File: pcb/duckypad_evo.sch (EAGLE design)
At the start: 93 parts, among them IC1 STM32F072C8T6, IC2 REG1117, IC3 74AHCT1G08DBV, SW1 324_SW324_SWITCH_FOOT_HOLE, SW10 KAILH_SWITCH_SOCKET_KAILH_SWI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, SW11 KAILH_SWITCH_SOCKET_KAILH_SWI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, SW12 KAILH_SWITCH_SOCKET_KAILH_SWI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, SW13 KAILH_SWITCH_SOCKET_KAILH_SWI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, SW14 KAILH_SWITCH_SOCKET_KAILH_SWI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, SW15 KAILH_SWITCH_SOCKET_KAILH_SWI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

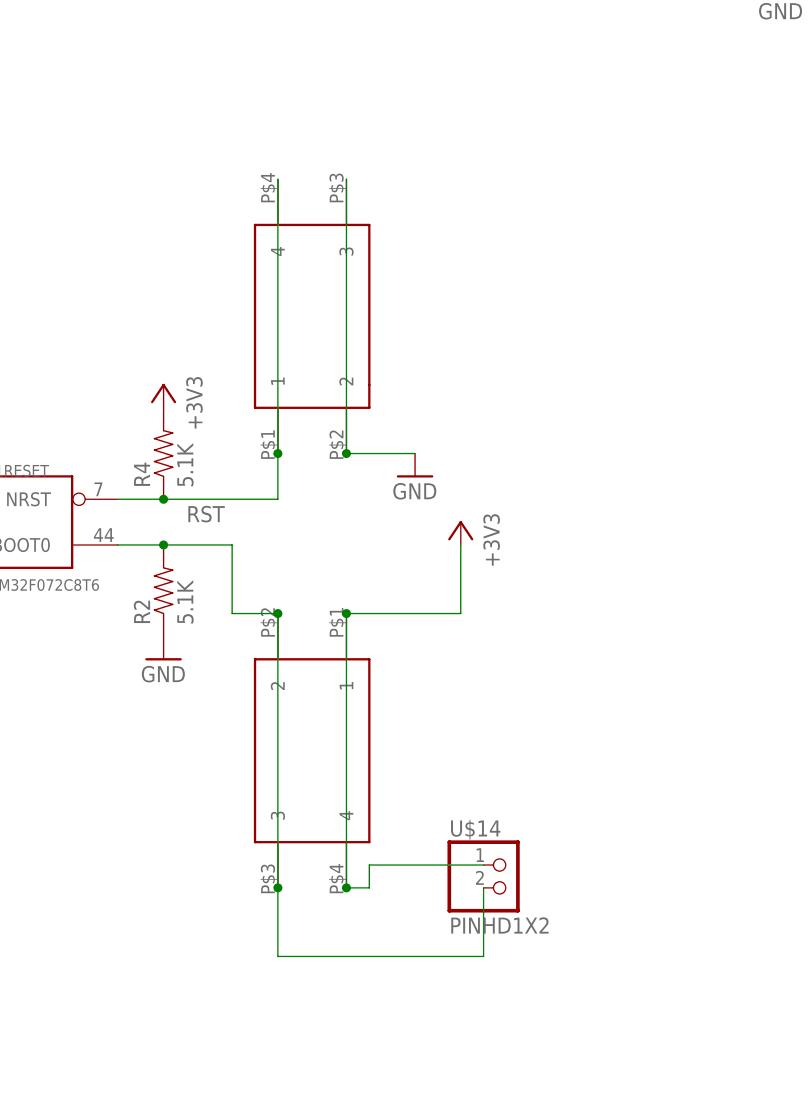
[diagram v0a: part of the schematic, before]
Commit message: new side-push buttons, new bugfix firmware
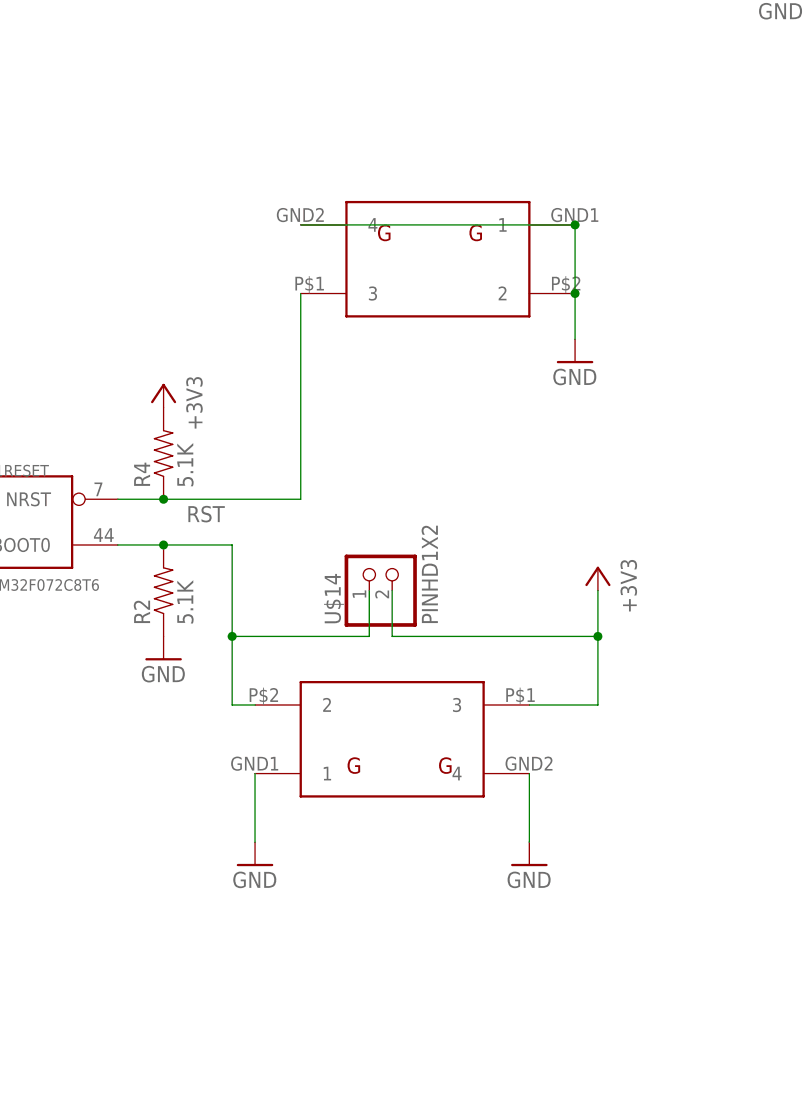
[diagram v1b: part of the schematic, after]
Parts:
- removed SW1, SW2: 324_SW324_SWITCH_FOOT_HOLE, 3pos_slide_switch:324_SW324_SWITCH_FOOT_HOLE
- added SW3, SW4: 3POS_SLIDE_SWITCH_324_SW, duckypad:3POS_SLIDE_SWITCH_324_SW
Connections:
- net +3V3: now also SW4.3, U$14.2; no longer SW1.1, SW1.4, U$14.1
- net BUTTON_DEBUG: now also SW4.2, U$14.1; no longer SW1.2, SW1.3, U$14.2
- net GND: now also SW3.1, SW3.2, SW3.4, SW4.1, SW4.4; no longer SW2.2, SW2.3
- net RST: now also SW3.3; no longer SW2.1, SW2.4
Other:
- moved on the sheet: U$14
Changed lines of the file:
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@@
 <part name="R1" library="joyAnalog" deviceset="RESISTOR" device="0805-RES" value="5.1K"/>
 <part name="R9" library="joyAnalog" deviceset="RESISTOR" device="0805-RES" value="5.1K"/>
-<part name="SW2" library="3pos_slide_switch" deviceset="324_SW" device="324_SWITCH_FOOT_HOLE" value="324_SW324_SWITCH_FOOT_HOLE"/>
-<part name="SW1" library="3pos_slide_switch" deviceset="324_SW" device="324_SWITCH_FOOT_HOLE" value="324_SW324_SWITCH_FOOT_HOLE"/>
 <part name="C28" library="clock" deviceset="CAP" device="0805" value="1uF"/>
 <part name="C29" library="clock" deviceset="CAP" device="0805" value="100nF"/>
@@
 <part name="P+3" library="supply1" library_urn="urn:adsk.eagle:library:371" deviceset="+5V" device=""/>
 <part name="+3V31" library="supply1" library_urn="urn:adsk.eagle:library:371" deviceset="+3V3" device=""/>
+<part name="SW3" library="duckypad" deviceset="3POS_SLIDE_SWITCH_324_SW" device="" value="3POS_SLIDE_SWITCH_324_SW"/>
+<part name="SW4" library="duckypad" deviceset="3POS_SLIDE_SWITCH_324_SW" device="" value="3POS_SLIDE_SWITCH_324_SW"/>
+<part name="GND17" library="supply1" library_urn="urn:adsk.eagle:library:371" deviceset="GND" device=""/>
+<part name="GND33" library="supply1" library_urn="urn:adsk.eagle:library:371" deviceset="GND" device=""/>
 </parts>
 <sheets>
@@
 <attribute name="VALUE" x="228.6" y="-170.18" size="1.778" layer="96" rot="MR90"/>
 </instance>
-<instance part="+3V7" gate="G$1" x="259.08" y="-180.34" smashed="yes" rot="MR0">
-<attribute name="VALUE" x="261.62" y="-185.42" size="1.778" layer="96" rot="MR90"/>
-</instance>
-<instance part="GND10" gate="1" x="254" y="-175.26" smashed="yes">
-<attribute name="VALUE" x="251.46" y="-177.8" size="1.778" layer="96"/>
+<instance part="+3V7" gate="G$1" x="274.32" y="-185.42" smashed="yes" rot="MR0">
+<attribute name="VALUE" x="276.86" y="-190.5" size="1.778" layer="96" rot="MR90"/>
+</instance>
+<instance part="GND10" gate="1" x="271.78" y="-162.56" smashed="yes">
+<attribute name="VALUE" x="269.24" y="-165.1" size="1.778" layer="96"/>
 </instance>
 <instance part="GND11" gate="1" x="172.72" y="-175.26" smashed="yes">
@@
 <attribute name="VALUE" x="-1.27" y="-153.162" size="1.778" layer="96" rot="MR0"/>
 </instance>
-<instance part="SW2" gate="G$1" x="241.3" y="-157.48" smashed="yes" rot="MR90"/>
-<instance part="SW1" gate="G$1" x="243.84" y="-205.74" smashed="yes" rot="MR270"/>
 <instance part="C28" gate="G$1" x="335.28" y="-2.54" smashed="yes" rot="R90">
 <attribute name="NAME" x="332.359" y="-1.016" size="1.778" layer="95" rot="R90"/>
@@
 <attribute name="NAME" x="152.4" y="-125.73" size="1.778" layer="95" rot="MR0"/>
 </instance>
-<instance part="U$14" gate="1" x="264.16" y="-220.98" smashed="yes">
-<attribute name="NAME" x="257.81" y="-215.265" size="1.778" layer="95"/>
-<attribute name="VALUE" x="257.81" y="-226.06" size="1.778" layer="96"/>
+<instance part="U$14" gate="1" x="251.46" y="-185.42" smashed="yes" rot="R90">
+<attribute name="NAME" x="245.745" y="-191.77" size="1.778" layer="95" rot="R90"/>
+<attribute name="VALUE" x="256.54" y="-191.77" size="1.778" layer="96" rot="R90"/>
 </instance>
 <instance part="SH1" gate="G$1" x="388.62" y="-256.54" smashed="yes"/>
@@
 <instance part="+3V31" gate="G$1" x="411.48" y="-264.16" smashed="yes" rot="MR0">
 <attribute name="VALUE" x="414.02" y="-269.24" size="1.778" layer="96" rot="MR90"/>
+</instance>
+<instance part="SW3" gate="G$1" x="256.54" y="-149.86" smashed="yes" rot="R180"/>
+<instance part="SW4" gate="G$1" x="251.46" y="-205.74" smashed="yes"/>
+<instance part="GND17" gate="1" x="236.22" y="-218.44" smashed="yes">
+<attribute name="VALUE" x="233.68" y="-220.98" size="1.778" layer="96"/>
+</instance>
+<instance part="GND33" gate="1" x="266.7" y="-218.44" smashed="yes">
+<attribute name="VALUE" x="264.16" y="-220.98" size="1.778" layer="96"/>
 </instance>
 </instances>
@@
 </segment>
 <segment>
-<pinref part="SW2" gate="G$1" pin="2"/>
-<pinref part="GND10" gate="1" pin="GND"/>
-<wire x1="246.38" y1="-172.72" x2="254" y2="-172.72" width="0.1524" layer="91"/>
-<pinref part="SW2" gate="G$1" pin="3"/>
-<wire x1="246.38" y1="-142.24" x2="246.38" y2="-172.72" width="0.1524" layer="91"/>
-<junction x="246.38" y="-172.72"/>
-</segment>
-<segment>
 <pinref part="GND11" gate="1" pin="GND"/>
 <wire x1="154.94" y1="-172.72" x2="172.72" y2="-172.72" width="0.1524" layer="91"/>
@@
 <wire x1="424.18" y1="-322.58" x2="370.84" y2="-322.58" width="0.1524" layer="91"/>
 <junction x="370.84" y="-322.58"/>
+</segment>
+<segment>
+<pinref part="SW3" gate="G$1" pin="2"/>
+<pinref part="GND10" gate="1" pin="GND"/>
+<wire x1="271.78" y1="-154.94" x2="271.78" y2="-160.02" width="0.1524" layer="91"/>
+<pinref part="SW3" gate="G$1" pin="1"/>
+<wire x1="271.78" y1="-154.94" x2="271.78" y2="-147.32" width="0.1524" layer="91"/>
+<junction x="271.78" y="-154.94"/>
+<pinref part="SW3" gate="G$1" pin="4"/>
+<wire x1="271.78" y1="-147.32" x2="241.3" y2="-147.32" width="0.1524" layer="91"/>
+<junction x="271.78" y="-147.32"/>
+</segment>
+<segment>
+<pinref part="SW4" gate="G$1" pin="1"/>
+<pinref part="GND17" gate="1" pin="GND"/>
+<wire x1="236.22" y1="-215.9" x2="236.22" y2="-208.28" width="0.1524" layer="91"/>
+</segment>
+<segment>
+<pinref part="SW4" gate="G$1" pin="4"/>
+<pinref part="GND33" gate="1" pin="GND"/>
+<wire x1="266.7" y1="-215.9" x2="266.7" y2="-208.28" width="0.1524" layer="91"/>
 </segment>
 </net>
@@
 <segment>
 <pinref part="+3V7" gate="G$1" pin="+3V3"/>
-<wire x1="246.38" y1="-190.5" x2="259.08" y2="-190.5" width="0.1524" layer="91"/>
-<wire x1="259.08" y1="-190.5" x2="259.08" y2="-182.88" width="0.1524" layer="91"/>
-<pinref part="SW1" gate="G$1" pin="1"/>
-<pinref part="SW1" gate="G$1" pin="4"/>
-<wire x1="246.38" y1="-190.5" x2="246.38" y2="-220.98" width="0.1524" layer="91"/>
-<junction x="246.38" y="-190.5"/>
-<pinref part="U$14" gate="1" pin="1"/>
-<wire x1="261.62" y1="-218.44" x2="248.92" y2="-218.44" width="0.1524" layer="91"/>
-<wire x1="248.92" y1="-218.44" x2="248.92" y2="-220.98" width="0.1524" layer="91"/>
-<wire x1="248.92" y1="-220.98" x2="246.38" y2="-220.98" width="0.1524" layer="91"/>
-<junction x="246.38" y="-220.98"/>
+<wire x1="274.32" y1="-200.66" x2="274.32" y2="-193.04" width="0.1524" layer="91"/>
+<pinref part="SW4" gate="G$1" pin="3"/>
+<wire x1="274.32" y1="-193.04" x2="274.32" y2="-187.96" width="0.1524" layer="91"/>
+<wire x1="274.32" y1="-200.66" x2="266.7" y2="-200.66" width="0.1524" layer="91"/>
+<pinref part="U$14" gate="1" pin="2"/>
+<wire x1="251.46" y1="-187.96" x2="251.46" y2="-193.04" width="0.1524" layer="91"/>
+<wire x1="251.46" y1="-193.04" x2="274.32" y2="-193.04" width="0.1524" layer="91"/>
+<junction x="274.32" y="-193.04"/>
 </segment>
 <segment>
@@
 <pinref part="R4" gate="G$1" pin="1"/>
 <wire x1="220.98" y1="-177.8" x2="226.06" y2="-177.8" width="0.1524" layer="91"/>
-<wire x1="226.06" y1="-177.8" x2="238.76" y2="-177.8" width="0.1524" layer="91"/>
+<wire x1="226.06" y1="-177.8" x2="241.3" y2="-177.8" width="0.1524" layer="91"/>
 <junction x="226.06" y="-177.8"/>
 <label x="228.6" y="-180.34" size="1.778" layer="95"/>
-<pinref part="SW2" gate="G$1" pin="1"/>
-<wire x1="238.76" y1="-177.8" x2="238.76" y2="-172.72" width="0.1524" layer="91"/>
-<pinref part="SW2" gate="G$1" pin="4"/>
-<wire x1="238.76" y1="-142.24" x2="238.76" y2="-172.72" width="0.1524" layer="91"/>
-<junction x="238.76" y="-172.72"/>
+<pinref part="SW3" gate="G$1" pin="3"/>
+<wire x1="241.3" y1="-177.8" x2="241.3" y2="-154.94" width="0.1524" layer="91"/>
 </segment>
 </net>
@@
 <wire x1="220.98" y1="-182.88" x2="226.06" y2="-182.88" width="0.1524" layer="91"/>
 <wire x1="226.06" y1="-182.88" x2="233.68" y2="-182.88" width="0.1524" layer="91"/>
-<wire x1="233.68" y1="-182.88" x2="233.68" y2="-190.5" width="0.1524" layer="91"/>
 <junction x="226.06" y="-182.88"/>
-<wire x1="233.68" y1="-190.5" x2="238.76" y2="-190.5" width="0.1524" layer="91"/>
-<pinref part="SW1" gate="G$1" pin="2"/>
-<pinref part="SW1" gate="G$1" pin="3"/>
-<wire x1="238.76" y1="-190.5" x2="238.76" y2="-220.98" width="0.1524" layer="91"/>
-<junction x="238.76" y="-190.5"/>
-<wire x1="261.62" y1="-228.6" x2="238.76" y2="-228.6" width="0.1524" layer="91"/>
-<wire x1="238.76" y1="-228.6" x2="238.76" y2="-220.98" width="0.1524" layer="91"/>
-<junction x="238.76" y="-220.98"/>
-<pinref part="U$14" gate="1" pin="2"/>
-<wire x1="261.62" y1="-220.98" x2="261.62" y2="-228.6" width="0.1524" layer="91"/>
-</segment>
-</net>
+<pinref part="SW4" gate="G$1" pin="2"/>
+<wire x1="233.68" y1="-182.88" x2="233.68" y2="-193.04" width="0.1524" layer="91"/>
+<wire x1="233.68" y1="-193.04" x2="233.68" y2="-200.66" width="0.1524" layer="91"/>
+<wire x1="233.68" y1="-200.66" x2="236.22" y2="-200.66" width="0.1524" layer="91"/>
+<pinref part="U$14" gate="1" pin="1"/>
+<wire x1="248.92" y1="-187.96" x2="248.92" y2="-193.04" width="0.1524" layer="91"/>
+<wire x1="248.92" y1="-193.04" x2="233.68" y2="-193.04" width="0.1524" layer="91"/>
+<junction x="233.68" y="-193.04"/>
+</segment>
+</net>
